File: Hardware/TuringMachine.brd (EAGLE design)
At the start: 100 x 49 mm, 70 parts, among them IC1 TL072, IC2 4015, IC3 4015, IC4 TL074, IC5 4016, T1 2N3904, T2 2N3904, T3 2N3904

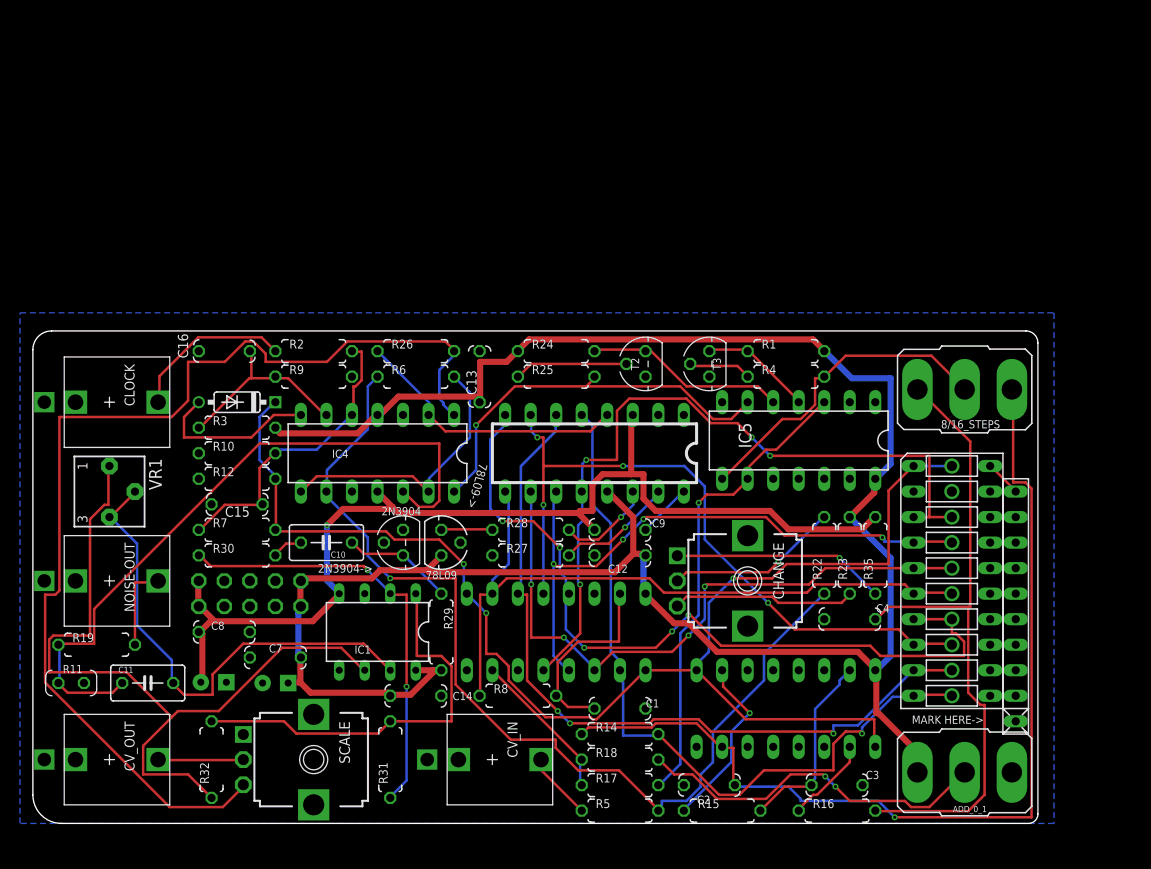
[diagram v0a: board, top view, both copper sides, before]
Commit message: Laid out & routed board with rotary switch
Need to print and check
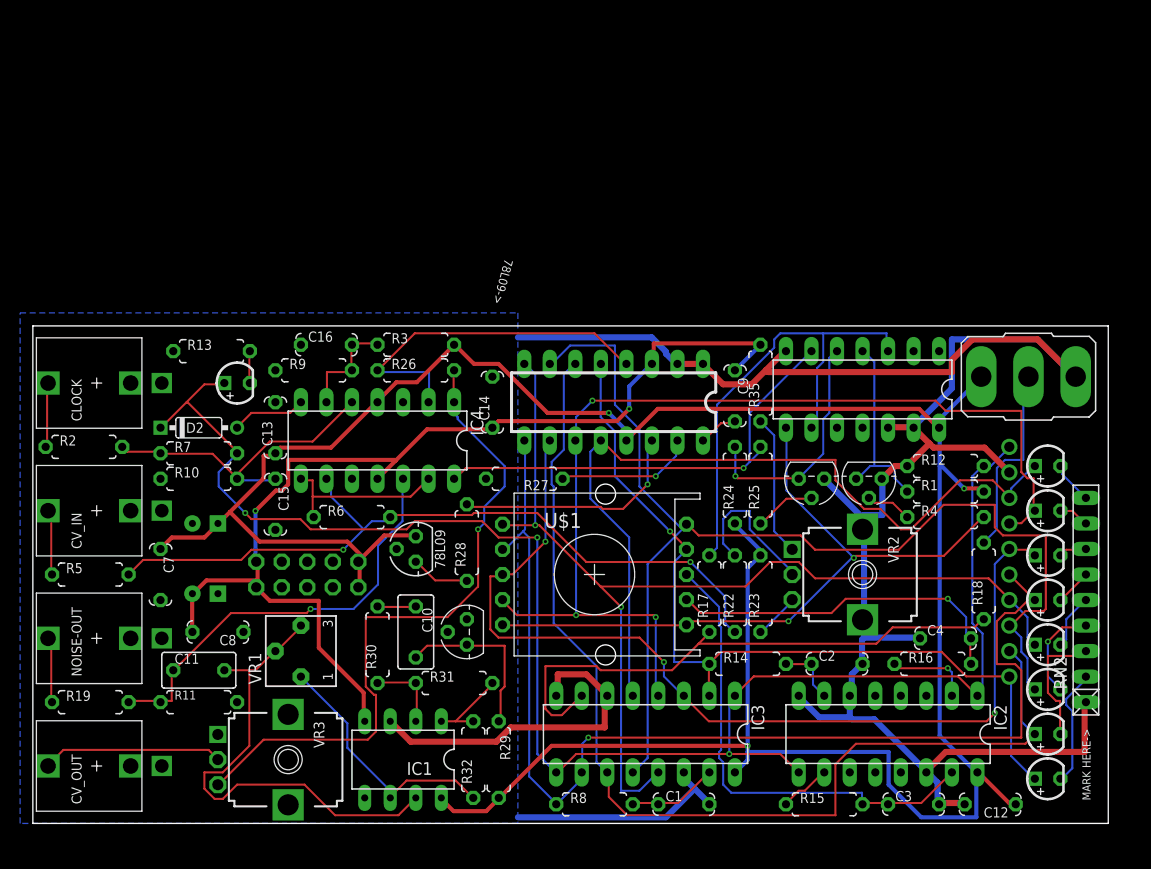
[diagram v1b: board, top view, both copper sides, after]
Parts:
- removed 8/16_STEPS: (no value), TomW:M9040P
- removed CHANGE, SCALE: 50k, TomW:EVUF
- removed DZ2: LB10, led:LB10
- removed RN1: 2.2k, TomW:RN-10
- added 1, 2, 3, 4, 5, 6, 7, 8, CLK: (no value), TomW:LED3MM
- added R13: 2.2k, TomW:0207/7
- added RN2: 2.2k, resistor-net:RN-9
- added U$1: ALPS-SRBV, TomW:ALPS-SRBV
- added VR2, VR3: (no value), MusicThingModular:9MM_SNAP-IN_POT
- D2: device TomW:DO35-7 -> MusicThingModular:DO35-7
- R11: device TomW:VERT-RESISTOR -> MusicThingModular:7MM_RESISTOR
- moved R12 70.5 mm to (90.8, 35.6)
- moved R5 57.7 mm to (5.71, 24.8)
- moved CV_IN 46.5 mm to (6.35, 31.1), turned to 90 degrees
- moved C12 44.4 mm to (95.2, 1.91)
- moved R18 40.3 mm to (94.6, 24.1), turned to 90 degrees
- moved ADD_0_1 39.9 mm to (99.1, 44.5)
- moved C14 30.2 mm to (45.7, 41.9), turned to 90 degrees
- moved R32 26.0 mm to (43.8, 6.35)
- moved VR1 24.8 mm to (26.7, 17.1), turned to 90 degrees
- moved R2 24.8 mm to (5.08, 37.5)
- moved R25 23.0 mm to (72.4, 33.7), turned to 90 degrees
- moved R24 22.2 mm to (69.8, 33.7), turned to 90 degrees
- moved R4 21.1 mm to (90.8, 30.5)
- moved R1 21.1 mm to (90.8, 33.0)
- moved R17 21.0 mm to (67.3, 22.9), turned to 90 degrees
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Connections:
- removed net N$17: 8/16_STEPS.1, C4.2, R16.2
- removed net N$18: C3.1, IC2.15, R15.2
- removed net N$9: 8/16_STEPS.3, C2.2, IC2.7, R14.1
- new net N$28: C2.1, IC2.7, R14.2
- new net STEP_12: C3.1, IC2.15, R15.2, U$1.G
- new net STEP_16: C4.2, R16.2, U$1.H
- net +12V: no longer C14.2
- net -12V: now also C14.1, C9.1; no longer C9.2
- net B1: now also 1.A, R14.1, U$1.F; no longer DZ2.10, R14.2
- net B2: now also 2.A; no longer DZ2.9
- net B3: now also 3.A, U$1.E; no longer DZ2.8
- net B4: now also 4.A, U$1.D; no longer DZ2.7
- net B5: now also 5.A, U$1.C; no longer DZ2.6
- net B6: now also 6.A, U$1.B; no longer DZ2.5
- net B7: now also 7.A, U$1.A; no longer DZ2.4
- net B8: now also 8.A; no longer DZ2.3
- net CLOCKIN: now also CLK.A; no longer DZ2.1
- net END_OF_LOOP: now also U$1.COM, U$1.COM2; no longer 8/16_STEPS.2
- net GND: now also C1.2, C14.2, C2.2, R13.1, R27.2, R9.1, RN2.1, VR2.M1, VR2.M2, VR3.1, VR3.M1, VR3.M2; no longer C1.1, C14.1, C2.1, R27.1, R9.2, RN1.1, SCALE.1
- net MAIN_OUT: now also VR3.3; no longer SCALE.3
- net N$10: now also C1.1; no longer C1.2
- net N$12: now also R9.2; no longer R9.1
- net N$15: now also CLK.K, R13.2; no longer DZ2.20, RN1.10
- net N$16: now also C10.2; no longer C10.1
- net N$20: now also C10.1; no longer C10.2
- net N$23: now also R27.1; no longer R27.2
- net N$25: now also C9.2; no longer C9.1
- net N$30: now also 8.K, RN2.9; no longer DZ2.18, RN1.9
- net N$31: now also 7.K, RN2.8; no longer DZ2.17, RN1.8
- net N$32: now also 6.K, RN2.7; no longer DZ2.16, RN1.7
- net N$33: now also 5.K, RN2.6; no longer DZ2.15, RN1.6
- net N$34: now also 4.K, RN2.5; no longer DZ2.14, RN1.5
- net N$35: now also 3.K, RN2.4; no longer DZ2.13, RN1.4
- net N$36: now also 2.K, RN2.3; no longer DZ2.12, RN1.3
- net N$37: now also 1.K, RN2.2; no longer DZ2.11, RN1.2
- net N$39: now also VR3.2; no longer SCALE.2
- net N$40: now also R19.1; no longer R19.2
- net N$43: now also VR2.2; no longer CHANGE.2
- net N$47: now also VR2.3; no longer CHANGE.3
- net N$48: now also VR2.1; no longer CHANGE.1
- net N$6: now also R6.2; no longer R6.1
- net N$7: now also R6.1; no longer R6.2
- net NOISE: now also R19.2; no longer R19.1
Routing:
- net GND: track 0.00 -> 248.9 mm
- net N$9: track 95.5 -> 0.00 mm, vias 1 -> 0
- net N$17: track 65.0 -> 0.00 mm
- net N$27: track 77.1 -> 25.5 mm
- net STEP_12: track 0.00 -> 48.2 mm
- net B3: track 69.9 -> 116.1 mm, vias 4 -> 0
- net +12V: track 219.5 -> 264.9 mm, vias 0 -> 3
- net B5: track 70.3 -> 113.6 mm, vias 0 -> 1
- net B7: track 61.6 -> 103.0 mm, vias 4 -> 3
- net MAIN_OUT: track 108.3 -> 67.0 mm, vias 0 -> 1
- net N$19: track 15.3 -> 56.4 mm
- net END_OF_LOOP: track 32.2 -> 68.1 mm, vias 0 -> 2
- net N$21: track 43.3 -> 7.79 mm, vias 2 -> 0
- net STEP_16: track 0.00 -> 34.6 mm, vias 0 -> 1
- net B6: track 64.0 -> 97.3 mm, vias 4 -> 3
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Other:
- board size 100 x 49 mm -> 107 x 49.5 mm
- board text removed: "2N3904->"

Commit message: tweaks
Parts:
- moved RN2 10.2 mm to (105.4, 12.1)
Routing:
- net MAIN_OUT: track 67.0 -> 99.7 mm, vias 1 -> 0
- net N$24: track 45.6 -> 64.3 mm, vias 1 -> 0
- net B7: track 103.0 -> 85.0 mm, vias 3 -> 4
- net GND: track 248.9 -> 233.1 mm
- net N$5: track 31.8 -> 47.5 mm
- net END_OF_LOOP: track 68.1 -> 82.8 mm, vias 2 -> 0
- net N$41: track 48.3 -> 34.6 mm
- net B3: track 116.1 -> 103.4 mm, vias 0 -> 1
- net N$6: track 76.1 -> 88.8 mm
- net N$30: track 4.33 -> 16.4 mm
- net N$19: track 56.4 -> 44.7 mm
- net B6: track 97.3 -> 85.8 mm
- net N$31: track 3.05 -> 12.9 mm
- net B5: track 113.6 -> 104.6 mm
- net STEP_16: track 34.6 -> 43.6 mm, vias 1 -> 0
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
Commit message: Hand routing
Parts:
- removed 78L09: (no value), v-reg:78LXX
- removed ADD_0_1: T-80-T-SPDT-ON-OFF-ON, TomW:M9040P
- removed IC4: TL074, linear:DIL14
- added C17: 1n, TomW:C050-024X044
- added C18: 0.47uf, rcl:C050-035X075
- added IC6, IC7: TL072P, TomW:DIL08
- added R20: 3.3k, TomW:0207/7
- added TL431: (no value), TomW:TO92-CLP
- added WRITE: T-80-T-SPDT-ON-OFF-ON, TomW:M9040P
- C12: value 100n -> 1n
- IC1: value TL072 -> TL072P
- R26: value 10k -> 5.1k
- R27, R28: value 10k -> 1.6k
- R3: value 100k -> 68k
- R7: value 1m -> 470k
- moved C4 77.4 mm to (40.0, 76.8)
- moved R16 70.7 mm to (26.7, 48.3)
- moved IC2 64.8 mm to (26.7, 36.8), turned to 270 degrees
- moved C2 64.5 mm to (17.8, 33.0)
- moved R12 63.6 mm to (33.7, 63.5)
- moved C3 60.7 mm to (35.6, 33.0), turned to 90 degrees
- moved R8 58.8 mm to (97.8, 43.2), turned to 90 degrees
- moved R14 58.6 mm to (15.9, 35.6)
- moved R15 56.0 mm to (33.0, 34.3), turned to 90 degrees
- moved C1 55.4 mm to (100.3, 44.5), turned to 90 degrees
- moved R18 49.4 mm to (50.8, 1.27), turned to 0 degrees
- moved R6 42.0 mm to (69.8, 12.7)
- moved IC3 41.3 mm to (90.2, 38.1), turned to 270 degrees
- moved R25 35.8 mm to (94.0, 5.08), turned to 0 degrees
- moved C11 35.8 mm to (50.8, 5.08)
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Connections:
- removed net N$38: 78L09.OUT, R28.1
- new net N$18: R20.1, R28.1, TL431.C, TL431.R
- new net N$9: C18.1, R32.1
- net +12V: now also IC6.8, IC7.8, R1.1, R20.2, R23.1, WRITE.1; no longer 78L09.IN, ADD_0_1.1, C12.1, IC4.4, R1.2, R23.2
- net -12V: now also IC6.4, IC7.4, R35.1; no longer IC4.11, R35.2
- net B1: now also R14.2; no longer R14.1
- net END_OF_LOOP: now also IC5.1, R4.1; no longer IC5.8, R4.2
- net GND: now also C1.1, C15.1, C3.1, IC5.5, IC5.6, IC6.3, IC7.3, R27.1, TL431.A, WRITE.3; no longer 78L09.GND, ADD_0_1.3, C1.2, C12.2, C15.2, C3.2, IC4.10, IC4.3, IC5.12, IC5.13, R27.2
- net MAIN_OUT: now also C17.2, IC7.1; no longer IC4.1
- net N$1: now also R4.2; no longer R4.1
- net N$10: now also C1.2; no longer C1.1
- net N$11: now also R18.1, WRITE.2; no longer ADD_0_1.2, R18.2
- net N$12: now also IC7.6; no longer IC4.6
- net N$13: now also C17.1, IC7.2; no longer IC4.2
- net N$16: now also C10.1; no longer C10.2
- net N$19: now also R18.2; no longer R18.1
- net N$20: now also C10.2, R30.1; no longer C10.1, R30.2
- net N$21: now also R30.2, R31.2; no longer R30.1, R31.1
- net N$22: now also C18.2, R31.1; no longer R31.2, R32.2
- net N$23: now also R27.2; no longer R27.1
- net N$24: now also IC5.13, IC6.7, R25.1; no longer IC4.14, IC5.6, R25.2
- net N$27: now also C12.1, R32.2; no longer R32.1
- net N$28: now also R14.1; no longer R14.2
- net N$4: now also IC5.11, R1.2; no longer IC5.4, R1.1
- net N$41: now also C11.1, C12.2; no longer C11.2
- net N$44: now also R25.2; no longer R25.1
- net N$45: now also IC5.12; no longer IC5.5
- net N$47: now also R23.2; no longer R23.1
- net N$48: now also R35.2; no longer R35.1
- net N$5: now also C15.2, IC7.5; no longer C15.1, IC4.5
- net N$6: now also IC6.2; no longer IC4.9
- net N$7: now also IC6.1, IC6.6; no longer IC4.13, IC4.8
- net N$8: now also IC7.7; no longer IC4.7
- net NOISE: now also C11.2, IC6.5; no longer C11.1, IC4.12
- net START_OF_LOOP: now also IC5.10, IC5.2; no longer IC5.3, IC5.9
- net STEP_12: now also C3.2; no longer C3.1
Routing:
- net GND: track 233.1 -> 0.00 mm
- net +12V: track 263.8 -> 80.4 mm, vias 2 -> 0
- net CLOCKIN: track 165.7 -> 0.00 mm, vias 1 -> 0
- net B4: track 111.1 -> 0.00 mm, vias 1 -> 0
- net B2: track 106.9 -> 0.00 mm
- net B3: track 103.4 -> 0.00 mm, vias 1 -> 0
- net B5: track 104.6 -> 9.94 mm, vias 1 -> 0
- net MAIN_OUT: track 99.7 -> 5.61 mm
- net B6: track 85.8 -> 0.00 mm, vias 3 -> 0
- net B7: track 85.0 -> 0.00 mm, vias 4 -> 0
- net B8: track 81.2 -> 0.00 mm, vias 1 -> 0
- net B1: track 90.5 -> 10.7 mm, vias 3 -> 0
- net N$6: track 88.8 -> 21.9 mm, vias 2 -> 0
- net -12V: track 104.2 -> 42.7 mm, vias 2 -> 0
- net END_OF_LOOP: track 82.8 -> 22.0 mm
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
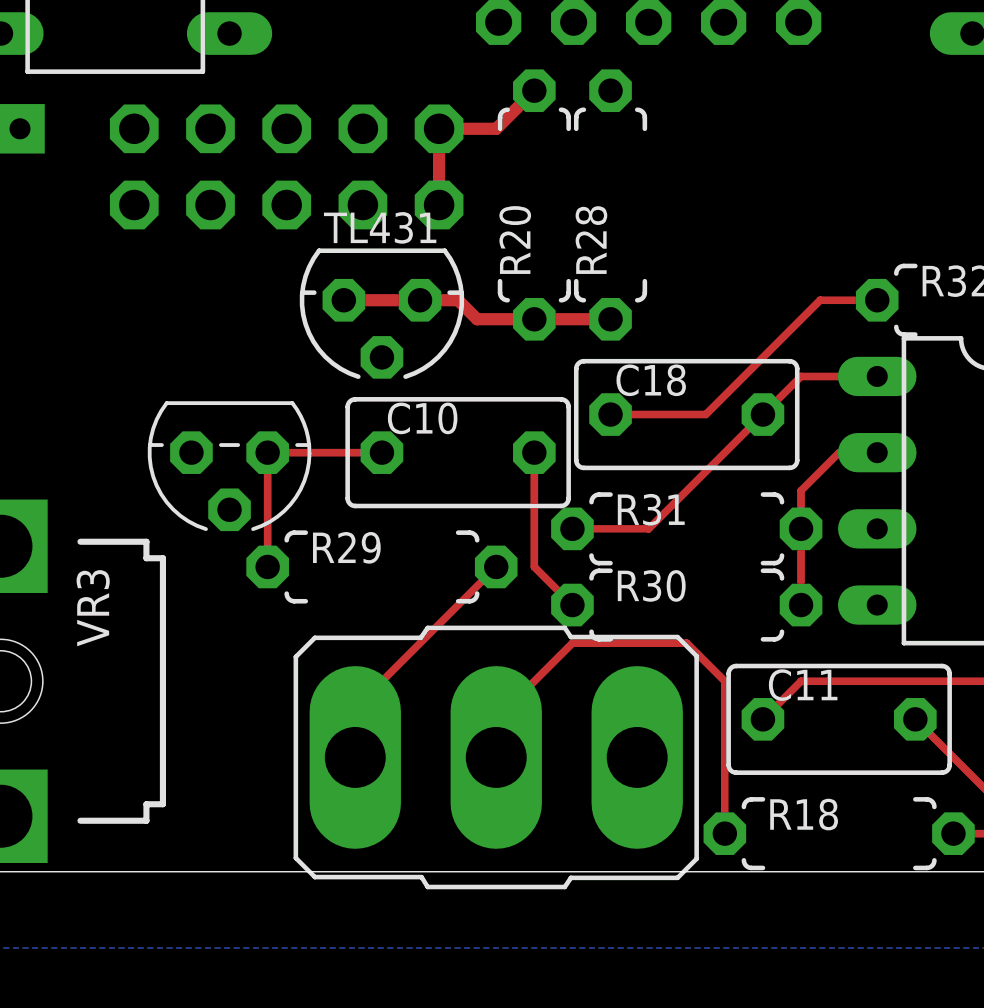
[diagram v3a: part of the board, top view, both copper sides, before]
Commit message: manual routing
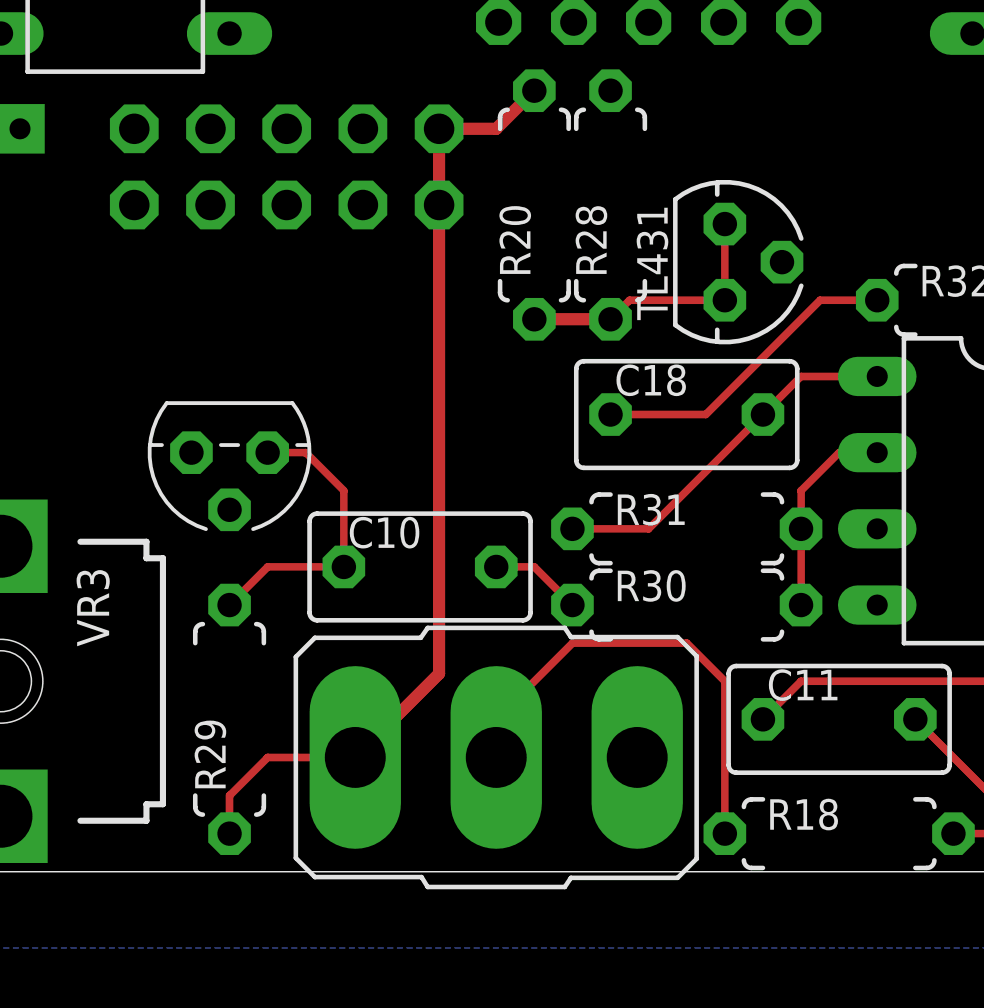
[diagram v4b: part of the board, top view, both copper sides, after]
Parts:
- moved TL431 11.5 mm to (47.0, 20.3), turned to 270 degrees
- moved R29 7.18 mm to (30.5, 5.08), turned to 90 degrees
- moved C10 4.02 mm to (36.8, 10.2)
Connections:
- net +12V: now also R29.1; no longer R29.2
- net N$16: now also R29.2; no longer R29.1
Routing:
- net +12V: track 80.4 -> 97.7 mm
- net N$20: track 5.61 -> 3.07 mm
- net N$16: track 7.62 -> 9.94 mm
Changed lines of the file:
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@@
 <element name="C9" library="TomW" package="C050-024X044" value="10n" x="59.055" y="48.26"/>
 <element name="T1" library="transistor" package="TO92" value="2N3904" x="30.48" y="13.97" rot="R180"/>
-<element name="R29" library="TomW" package="0207/7" value="100k" x="35.56" y="10.16"/>
-<element name="C10" library="rcl" package="C050-035X075" value="0.47uf" x="38.1" y="13.97"/>
+<element name="R29" library="TomW" package="0207/7" value="100k" x="30.48" y="5.08" rot="R90"/>
+<element name="C10" library="rcl" package="C050-035X075" value="0.47uf" x="36.83" y="10.16"/>
 <element name="R30" library="TomW" package="0207/7" value="10k" x="45.72" y="8.89"/>
 <element name="R31" library="TomW" package="0207/7" value="470k" x="45.72" y="11.43"/>
@@
 <element name="VR3" library="MusicThingModular" package="9MM_SNAP-IN_POT" value="" x="22.86" y="6.35" locked="yes" rot="R270"/>
 <element name="C17" library="TomW" package="C050-024X044" value="1n" x="71.12" y="45.72" rot="R90"/>
-<element name="TL431" library="TomW" package="TO92-CLP" value="" x="35.56" y="19.05" rot="R180"/>
+<element name="TL431" library="TomW" package="TO92-CLP" value="" x="46.99" y="20.32" rot="R270"/>
 <element name="R20" library="TomW" package="0207/7" value="3.3k" x="40.64" y="22.225" rot="R90"/>
 <element name="C18" library="rcl" package="C050-035X075" value="0.47uf" x="45.72" y="15.24"/>
@@
 <contactref element="POWER" pad="10"/>
 <contactref element="U$2" pad="13"/>
-<contactref element="R29" pad="2"/>
+<contactref element="R29" pad="1"/>
 <contactref element="R3" pad="2"/>
 <contactref element="WRITE" pad="1"/>
@@
 <wire x1="74.93" y1="19.05" x2="74.93" y2="11.43" width="0.254" layer="1"/>
 <wire x1="74.93" y1="11.43" x2="73.66" y2="10.16" width="0.254" layer="1"/>
+<wire x1="30.48" y1="1.27" x2="30.48" y2="2.54" width="0.254" layer="1"/>
+<wire x1="30.48" y1="2.54" x2="31.75" y2="3.81" width="0.254" layer="1"/>
+<wire x1="31.75" y1="3.81" x2="34.671" y2="3.81" width="0.254" layer="1"/>
+<wire x1="37.465" y1="22.225" x2="37.465" y2="6.604" width="0.4064" layer="1"/>
+<wire x1="37.465" y1="6.604" x2="34.671" y2="3.81" width="0.4064" layer="1"/>
 <wire x1="81.28" y1="46.99" x2="93.98" y2="46.99" width="0" layer="19" extent="1-1"/>
 <wire x1="76.2" y1="20.32" x2="76.2" y2="38.1" width="0" layer="19" extent="1-1"/>
 <wire x1="66.04" y1="20.32" x2="74.93" y2="19.05" width="0" layer="19" extent="1-1"/>
 <wire x1="40.64" y1="26.035" x2="57.15" y2="19.05" width="0" layer="19" extent="1-1"/>
-<wire x1="39.37" y1="10.16" x2="37.465" y2="22.225" width="0" layer="19" extent="1-1"/>
 <wire x1="23.495" y1="24.765" x2="37.465" y2="24.765" width="0" layer="19" extent="1-1"/>
 <wire x1="30.48" y1="45.72" x2="37.465" y2="24.765" width="0" layer="19" extent="1-1"/>
@@
 <wire x1="21.59" y1="53.975" x2="30.48" y2="56.515" width="0" layer="19" extent="1-1"/>
 <wire x1="39.37" y1="52.07" x2="30.48" y2="56.515" width="0" layer="19" extent="1-1"/>
-<wire x1="34.671" y1="3.81" x2="34.671" y2="5.461" width="0.254" layer="1"/>
-<wire x1="34.671" y1="5.461" x2="39.37" y2="10.16" width="0.254" layer="1"/>
 </signal>
 <signal name="N$2">
@@
 <signal name="N$16">
 <contactref element="T1" pad="3"/>
-<contactref element="R29" pad="1"/>
+<contactref element="R29" pad="2"/>
 <contactref element="C10" pad="1"/>
-<wire x1="31.75" y1="13.97" x2="31.75" y2="10.16" width="0.254" layer="1"/>
-<wire x1="31.75" y1="13.97" x2="35.56" y2="13.97" width="0.254" layer="1"/>
+<wire x1="34.29" y1="10.16" x2="31.75" y2="10.16" width="0.254" layer="1"/>
+<wire x1="31.75" y1="10.16" x2="30.48" y2="8.89" width="0.254" layer="1"/>
+<wire x1="31.75" y1="13.97" x2="33.02" y2="13.97" width="0.254" layer="1"/>
+<wire x1="33.02" y1="13.97" x2="34.29" y2="12.7" width="0.254" layer="1"/>
+<wire x1="34.29" y1="12.7" x2="34.29" y2="10.16" width="0.254" layer="1"/>
 </signal>
 <signal name="N$20">
 <contactref element="C10" pad="2"/>
 <contactref element="R30" pad="1"/>
-<wire x1="40.64" y1="13.97" x2="40.64" y2="10.16" width="0.254" layer="1"/>
+<wire x1="39.37" y1="10.16" x2="40.64" y2="10.16" width="0.254" layer="1"/>
 <wire x1="40.64" y1="10.16" x2="41.91" y2="8.89" width="0.254" layer="1"/>
 </signal>
@@
 <contactref element="R20" pad="1"/>
 <wire x1="43.18" y1="18.415" x2="40.64" y2="18.415" width="0.4064" layer="1"/>
-<wire x1="40.64" y1="18.415" x2="38.735" y2="18.415" width="0.4064" layer="1"/>
-<wire x1="38.735" y1="18.415" x2="38.1" y2="19.05" width="0.4064" layer="1"/>
-<wire x1="38.1" y1="19.05" x2="36.83" y2="19.05" width="0.4064" layer="1"/>
-<wire x1="36.83" y1="19.05" x2="34.29" y2="19.05" width="0.4064" layer="1"/>
+<wire x1="46.99" y1="19.05" x2="43.815" y2="19.05" width="0.254" layer="1"/>
+<wire x1="43.815" y1="19.05" x2="43.18" y2="18.415" width="0.254" layer="1"/>
+<wire x1="46.99" y1="21.59" x2="46.99" y2="19.05" width="0.254" layer="1"/>
 </signal>
 <signal name="N$9">
